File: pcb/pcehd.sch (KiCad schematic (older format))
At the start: 3 parts, among them U1 AP7361

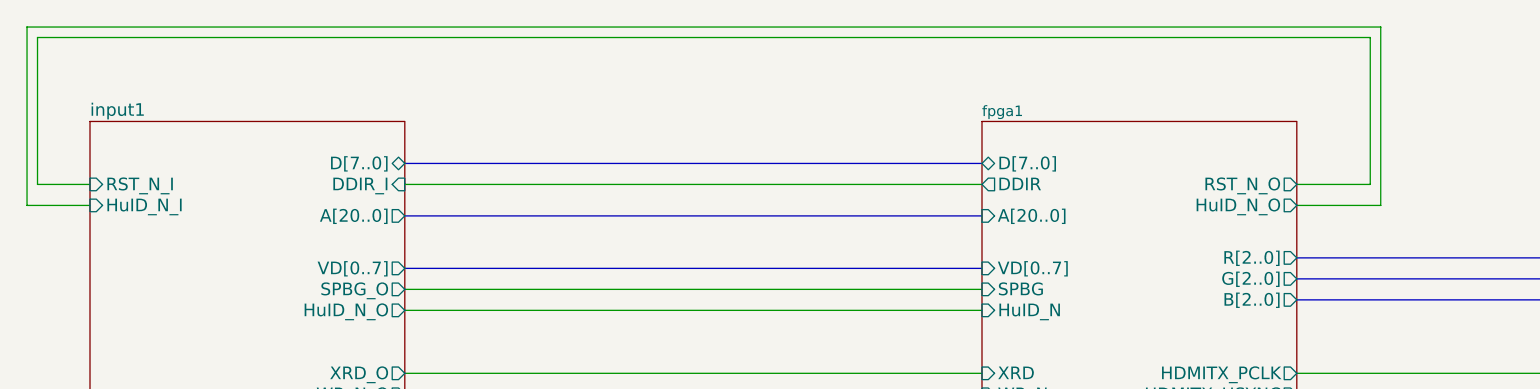
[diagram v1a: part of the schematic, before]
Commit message: Added CDD signal to last open IO pin
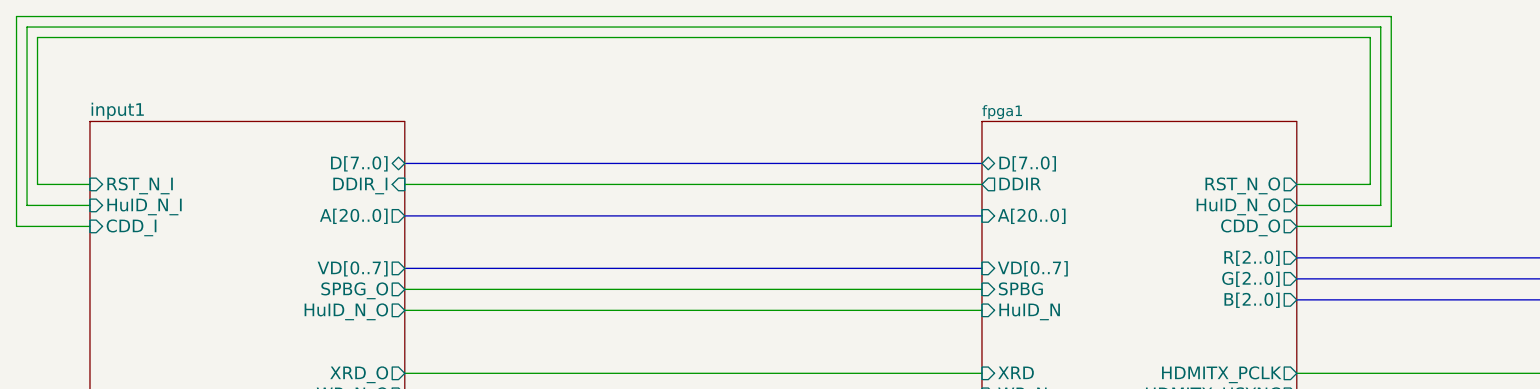
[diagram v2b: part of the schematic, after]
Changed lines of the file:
@@
 Sheet 1 5
 Title "PCEHD"
-Date "2020-01-15"
+Date "2020-01-18"
 Rev "0.1"
 Comp ""
@@
 F27 "G[2..0]" O R 7350 2600 60
 F28 "B[2..0]" O R 7350 2700 60
+F29 "CDD_O" O R 7350 2350 60
 $EndSheet
 $Sheet
@@
 F16 "HuID_N_O" O R 3100 2750 60
 F17 "XRD_O" O R 3100 3050 60
+F18 "CDD_I" I L 1600 2350 60
 $EndSheet
 Wire Wire Line
@@
 Wire Wire Line
 	5700 6100 6300 6100
+Wire Wire Line
+	7350 2350 7800 2350
+Wire Wire Line
+	7800 2350 7800 1350
+Wire Wire Line
+	7800 1350 1250 1350
+Wire Wire Line
+	1250 1350 1250 2350
+Wire Wire Line
+	1250 2350 1600 2350
 $EndSCHEMATC

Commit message: Finished version 0.1
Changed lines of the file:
@@
 F1 "input2.sch" 60
 F2 "DCK" I L 3700 4200 60
-F3 "HSn" I L 3700 4300 60
-F4 "DVDD5V" O R 5200 5600 60
-F5 "DCKFB_I" I R 5200 4200 60
-F6 "SDA" B R 5200 4900 60
-F7 "SCL" I R 5200 5000 60
-F8 "SI_CLK1_O" O R 5200 4400 60
-F9 "IS2_DATA" O R 5200 5150 60
-F10 "IS2_BCK" O R 5200 5250 60
-F11 "IS2_WS" O R 5200 5350 60
-F12 "SI_CLK0_O" O R 5200 4300 60
-F13 "VCCIO" I L 3700 5600 60
+F3 "DVDD5V" O R 5200 5600 60
+F4 "DCKFB_I" I R 5200 4200 60
+F5 "SDA" B R 5200 4900 60
+F6 "SCL" I R 5200 5000 60
+F7 "SI_CLK1_O" O R 5200 4400 60
+F8 "IS2_DATA" O R 5200 5150 60
+F9 "IS2_BCK" O R 5200 5250 60
+F10 "IS2_WS" O R 5200 5350 60
+F11 "SI_CLK0_O" O R 5200 4300 60
+F12 "VCCIO" I L 3700 5600 60
+F13 "HSn_buf" I L 3700 4300 60
 $EndSheet
 $Sheet
